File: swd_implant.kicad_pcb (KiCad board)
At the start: 2 copper layers, 13.9 x 38.5 mm, 25 parts, among them J1 U262-161N-4BVC11, J2 G&W pressure contact, J3 50 mil Pin Header, J4 SOICbite, J5 100 mil Pin Header, J6 100 mil Pin header, U1 ATSAMD21E18A, U2 AP2127K-3.3

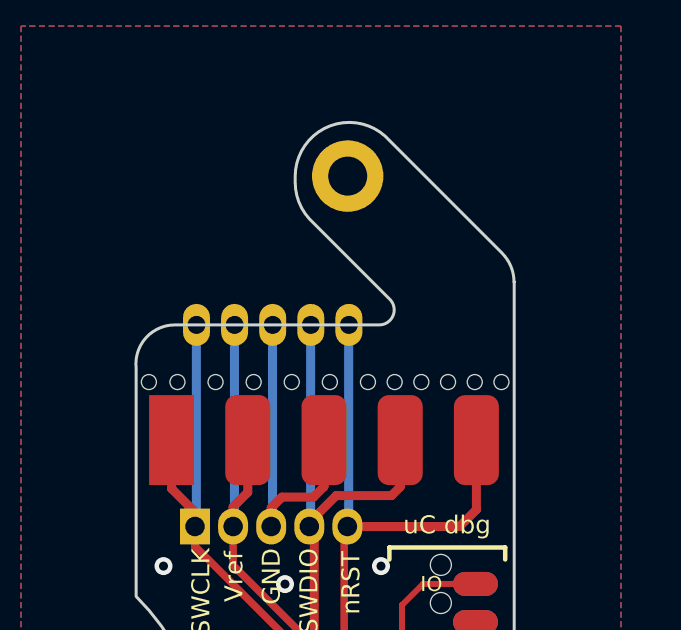
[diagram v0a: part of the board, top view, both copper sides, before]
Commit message: Add Z marker to front of board
This Z is to indicate that it is the "Zelda" variant of the implant
board.
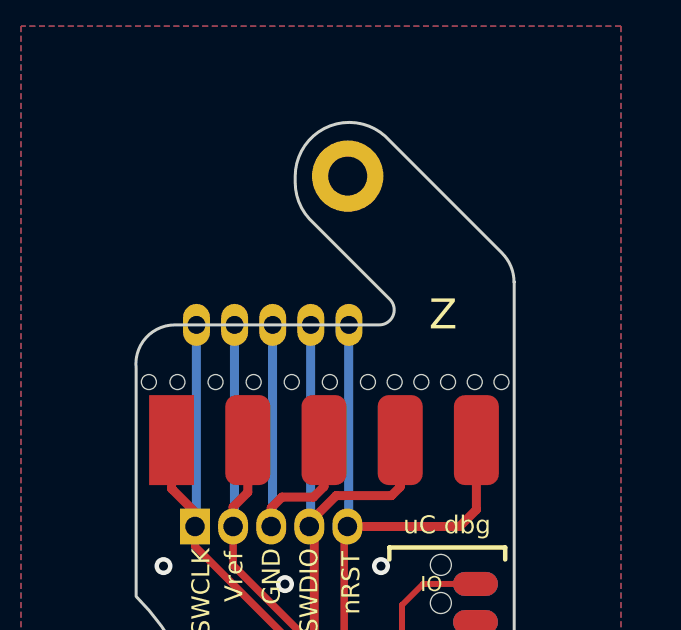
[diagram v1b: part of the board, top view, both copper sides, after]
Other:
- board text added: "Z"
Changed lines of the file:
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@@
 		)
 	)
-	(property "VERSION" "Mario")
+	(property "VERSION" "Zelda")
 	(net 0 "")
 	(net 1 "GND")
@@
 		)
 	)
+	(gr_text "Z"
+		(at 63.6 100.2 0)
+		(layer "F.SilkS")
+		(effects
+			(font
+				(size 1 1)
+				(thickness 0.15)
+			)
+			(justify left bottom)
+		)
+	)

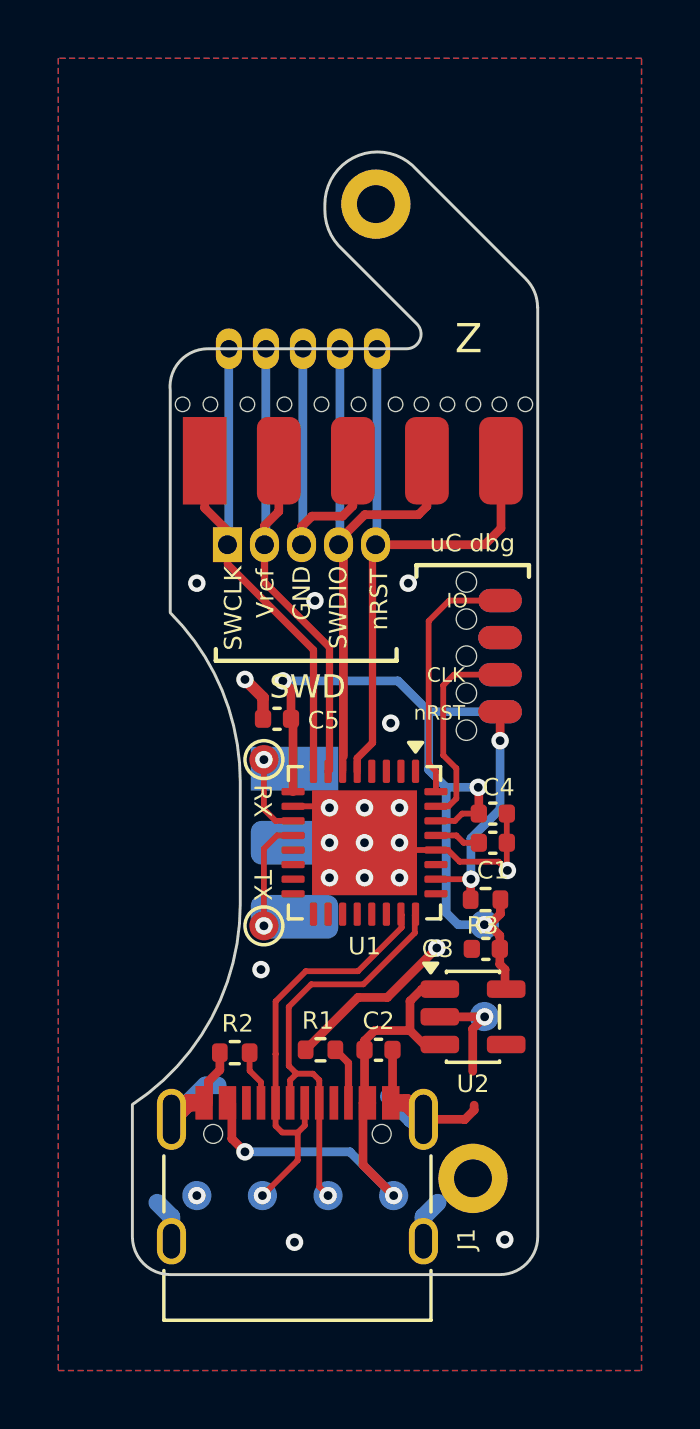
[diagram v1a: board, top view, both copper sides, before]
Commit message: Add Zelda version of implant
Just changed the board shape to fit the altered location of the SWD pins
on that version.
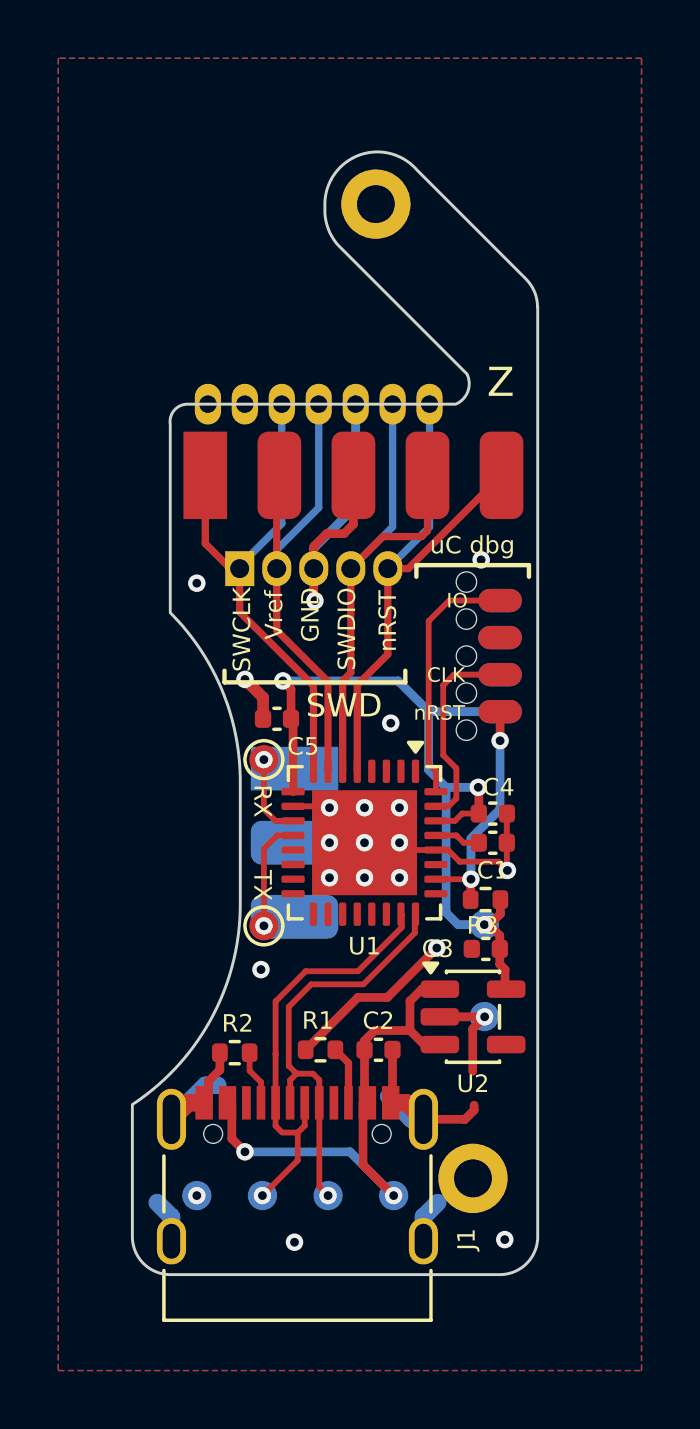
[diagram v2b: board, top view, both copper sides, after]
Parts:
- J2: value G&W pressure contact -> G&W Board Zelda; footprint GnW_SWD:GnW_SWD -> GnW_SWD:GnW_SWD_z
- moved J3 0.92 mm to (56.2, 107.5)
- moved Ref** 0.60 mm to (60.2, 105.3)
- moved J5 0.50 mm to (60.1, 105.8)
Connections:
- J2 pad 6: (no net) -> GND
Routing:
- net /GnW_NRST: track 21.8 -> 18.8 mm
- net /GnW_SWDIO: track 20.2 -> 18.4 mm
- net /GnW_Vref: track 18.6 -> 17.2 mm
- net /GnW_SWCLK: track 19.0 -> 18.1 mm
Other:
- outline, holes or cut-outs redrawn

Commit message: Prep for fabrication
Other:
- board text added: "${TITLE} ${VERSION}"
- board text added: "JLCJLCJLC"
- board text added: "REV:${REV}"
- board text removed: "G&W ${VERSION}"
- board text removed: "Z"
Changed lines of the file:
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@@
 	)
 	(paper "A4")
+	(title_block
+		(title "${TITLE}")
+		(rev "${REV}")
+		(comment 1 "${VERSION}")
+	)
 	(layers
 		(0 "F.Cu" signal)
@@
 		)
 	)
+	(property "REV" "z1")
+	(property "TITLE" "G&W_SWD")
 	(property "VERSION" "Zelda")
 	(net 0 "")
@@
 		(sheetname "/")
 		(sheetfile "swd_implant.kicad_sch")
-		(attr exclude_from_pos_files)
+		(attr exclude_from_pos_files exclude_from_bom)
 		(fp_circle
 			(center 0 0)
@@
 		(sheetname "/")
 		(sheetfile "swd_implant.kicad_sch")
-		(attr through_hole)
+		(attr through_hole exclude_from_bom)
 		(fp_poly
 			(pts
@@
 		(sheetname "/")
 		(sheetfile "swd_implant.kicad_sch")
-		(attr exclude_from_pos_files)
+		(attr exclude_from_pos_files exclude_from_bom)
 		(fp_circle
 			(center 0 0)
@@
 		(sheetname "/")
 		(sheetfile "swd_implant.kicad_sch")
-		(attr through_hole)
+		(attr through_hole exclude_from_pos_files exclude_from_bom)
 		(fp_line
 			(start 1.55 -1.15)
@@
 		(sheetname "/")
 		(sheetfile "swd_implant.kicad_sch")
-		(attr through_hole)
+		(attr through_hole exclude_from_pos_files exclude_from_bom)
 		(fp_line
 			(start 1.27 0.381)
@@
 		(sheetname "/")
 		(sheetfile "swd_implant.kicad_sch")
-		(attr exclude_from_pos_files)
+		(attr exclude_from_pos_files exclude_from_bom)
 		(fp_circle
 			(center 0 0)
@@
 		(sheetname "/")
 		(sheetfile "swd_implant.kicad_sch")
-		(attr exclude_from_pos_files)
+		(attr exclude_from_pos_files exclude_from_bom)
 		(fp_circle
 			(center 0 0)
@@
 		(sheetname "/")
 		(sheetfile "swd_implant.kicad_sch")
-		(attr exclude_from_pos_files)
+		(attr exclude_from_pos_files exclude_from_bom)
 		(fp_circle
 			(center 0 0)
@@
 		)
 	)
-	(gr_text "Z"
-		(at 64.7 101.7 0)
+	(gr_text "REV:${REV}"
+		(at 61.4 96.9 315)
 		(layer "F.SilkS")
 		(effects
@@
 		)
 	)
-	(gr_text "G&W ${VERSION}"
-		(at 66 104.4 0)
+	(gr_text "${TITLE} ${VERSION}"
+		(at 66.2 104.4 0)
 		(layer "B.SilkS")
 		(effects
@@
 		)
 	)
+	(gr_text "JLCJLCJLC"
+		(at 65.3 125.1 0)
+		(layer "B.SilkS")
+		(effects
+			(font
+				(size 1 1)
+				(thickness 0.15)
+			)
+			(justify left bottom mirror)
+		)
+	)
 	(gr_text "GND"
 		(at 55 129.66 90)
@@
 	)
 	(gr_text "GND"
-		(at 63.24 122.94 90)
+		(at 63.3 122.6 90)
 		(layer "B.SilkS")
 		(effects

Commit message: Add LCSC part numbers
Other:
- board text added: "JLCJLCJLCJLC"
- board text removed: "JLCJLCJLC"
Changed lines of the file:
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@@
 	(generator_version "9.0")
 	(general
-		(thickness 0.59)
+		(thickness 0.69)
 		(legacy_teardrops no)
 	)
@@
 			(layer "F.Mask"
 				(type "Top Solder Mask")
-				(color "Green")
+				(color "Purple")
 				(thickness 0.01)
 				(material "Dry Film")
@@
 			(layer "dielectric 1"
 				(type "core")
-				(color "Polyimide")
-				(thickness 0.5)
-				(material "Polyimide")
-				(epsilon_r 3.2)
-				(loss_tangent 0.004)
+				(color "FR4 natural")
+				(thickness 0.6)
+				(material "FR4")
+				(epsilon_r 4.5)
+				(loss_tangent 0.02)
 			)
 			(layer "B.Cu"
@@
 			(layer "B.Mask"
 				(type "Bottom Solder Mask")
-				(color "Green")
+				(color "Purple")
 				(thickness 0.01)
 				(material "Dry Film")
@@
 		(sheetname "/")
 		(sheetfile "swd_implant.kicad_sch")
-		(attr through_hole exclude_from_bom)
+		(attr through_hole exclude_from_pos_files exclude_from_bom)
 		(fp_poly
 			(pts
@@
 		(sheetname "/")
 		(sheetfile "swd_implant.kicad_sch")
-		(attr through_hole)
+		(attr through_hole exclude_from_pos_files exclude_from_bom)
 		(pad "1" smd rect
 			(at -5.08 -1.5)
@@
 		(sheetname "/")
 		(sheetfile "swd_implant.kicad_sch")
-		(attr exclude_from_pos_files)
+		(attr exclude_from_pos_files exclude_from_bom)
 		(fp_circle
 			(center 0 0)
@@
 			)
 		)
-		(attr through_hole)
+		(attr through_hole exclude_from_pos_files exclude_from_bom)
 		(fp_poly
 			(pts
@@
 		(sheetname "/")
 		(sheetfile "swd_implant.kicad_sch")
-		(attr through_hole)
+		(attr through_hole exclude_from_pos_files exclude_from_bom)
 		(pad "1" smd rect
 			(at -2.54 1.5 270)
@@
 		(sheetname "/")
 		(sheetfile "swd_implant.kicad_sch")
-		(attr exclude_from_pos_files)
+		(attr exclude_from_pos_files exclude_from_bom)
 		(fp_circle
 			(center 0 0)
@@
 		(sheetname "/")
 		(sheetfile "swd_implant.kicad_sch")
-		(attr exclude_from_pos_files)
+		(attr exclude_from_pos_files exclude_from_bom)
 		(fp_circle
 			(center 0 0)
@@
 		)
 	)
-	(gr_text "JLCJLCJLC"
+	(gr_text "JLCJLCJLCJLC"
 		(at 65.3 125.1 0)
 		(layer "B.SilkS")

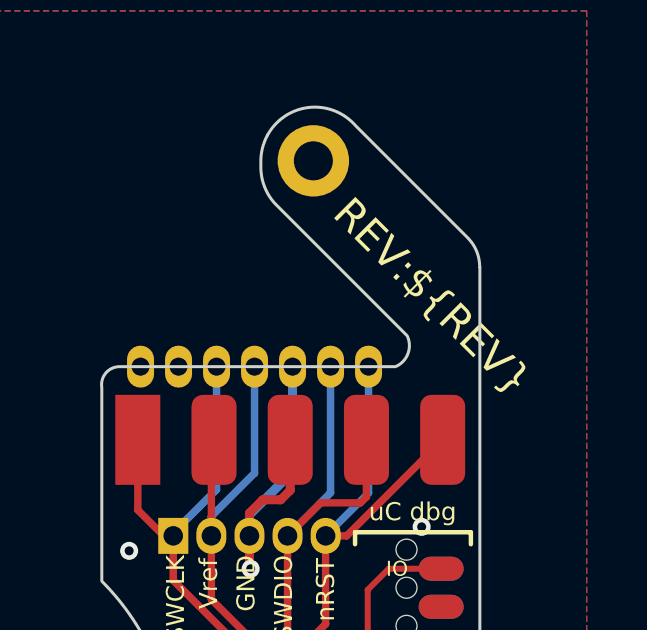
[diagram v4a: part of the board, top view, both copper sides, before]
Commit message: Add logos
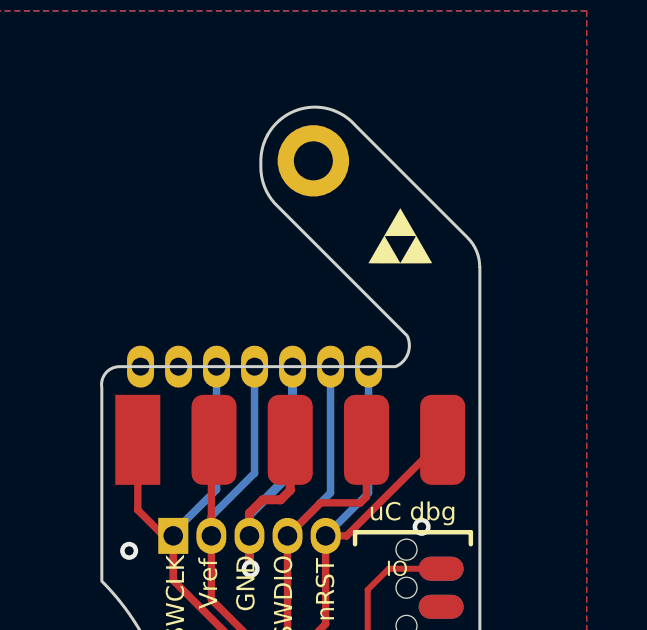
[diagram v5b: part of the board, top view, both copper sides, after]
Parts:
- added G***: LOGO, LOGO, F.Cu at (63.8, 97.5)
- added Q**: Qwindelzorf, qwindelzorf:qwindelzorf_1520, B.Cu at (70.7, 87.3)
